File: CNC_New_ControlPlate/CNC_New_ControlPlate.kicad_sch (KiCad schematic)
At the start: 5 parts, among them J1 OTHER

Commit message: [*] Исправлены ошибки с выходами питания. [+] Добавлены обозначения элементов
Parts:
- gave numbers to parts that had none: 4
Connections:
- no-connect marks 0 -> 22

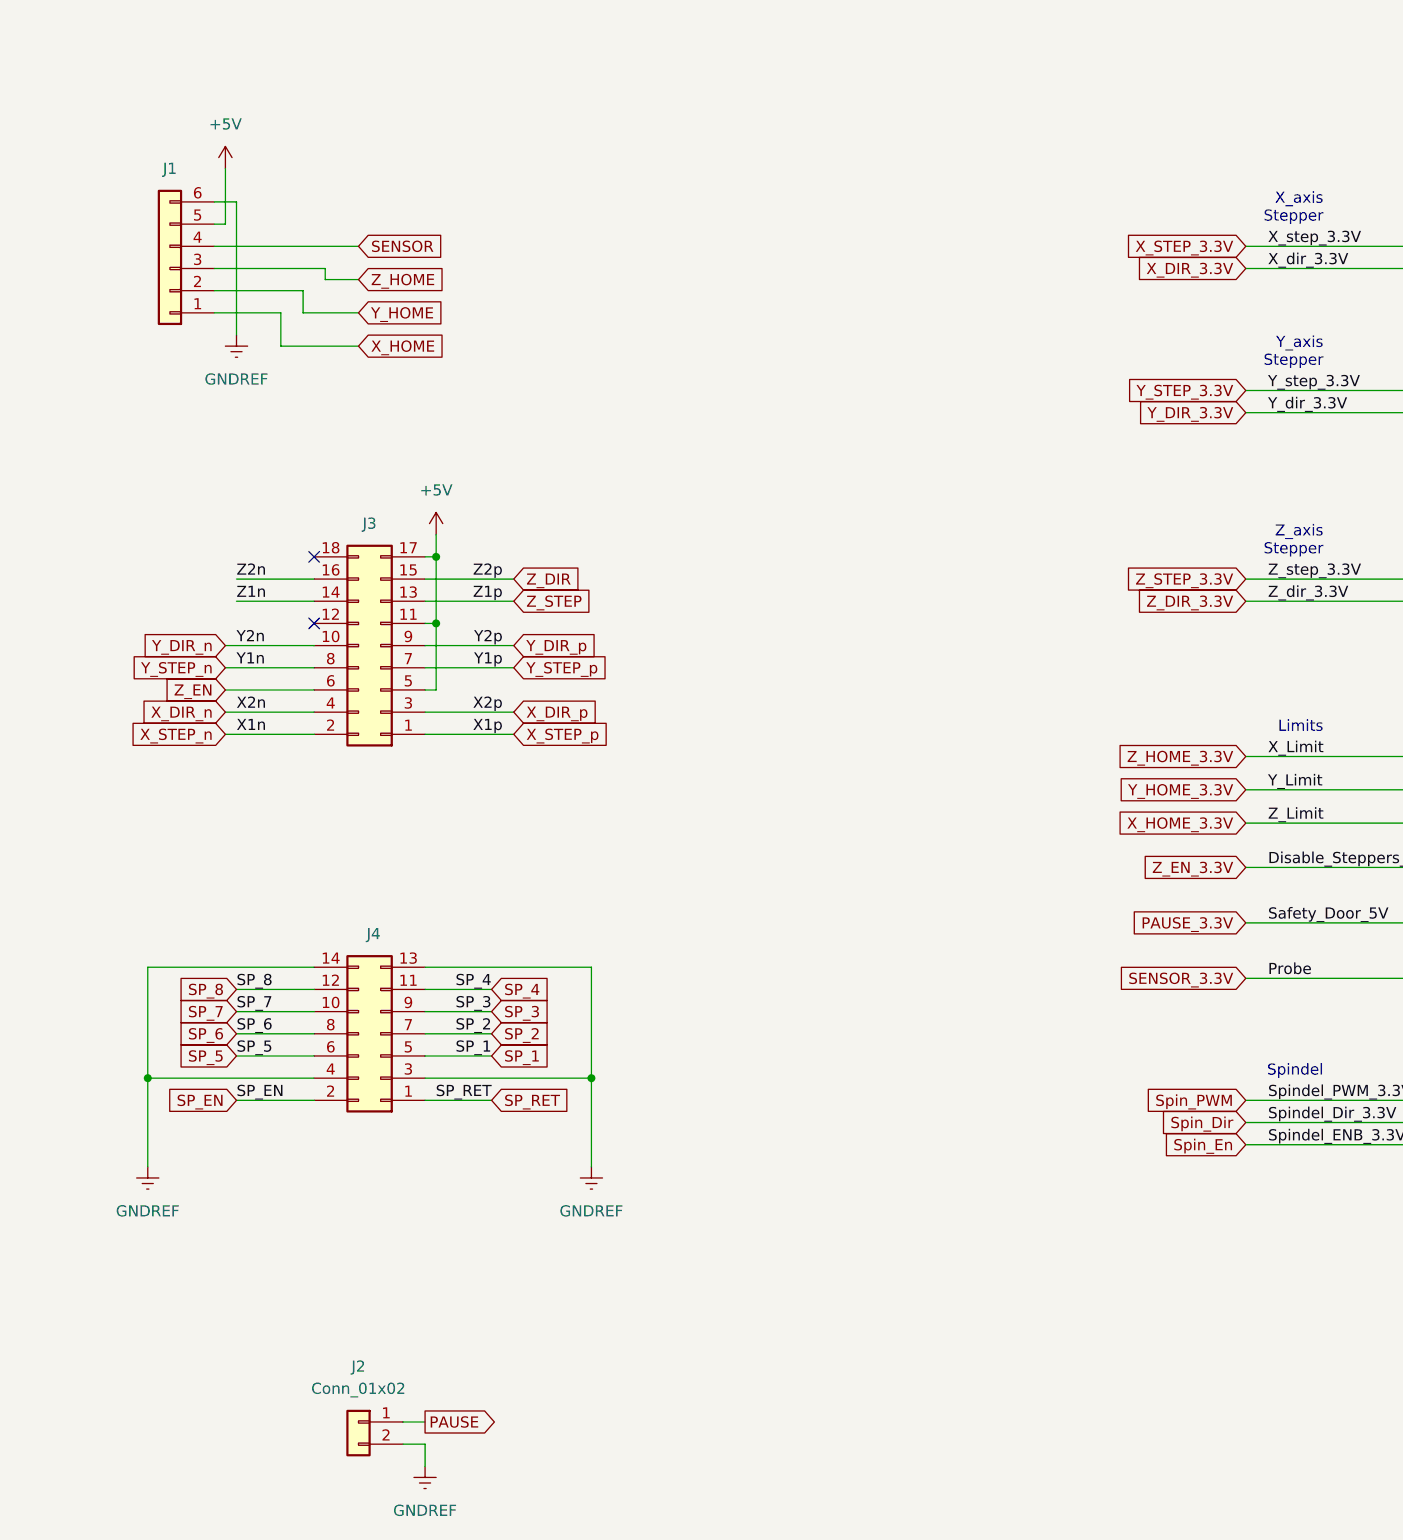
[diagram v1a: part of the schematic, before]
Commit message: [*] Порядок выводов на разъёме Others [*] Порядок выводов на разъёме Pause [*] Порядок подключения каналов на драйвере диф. линий [+] Начата расстановка pcb схемы
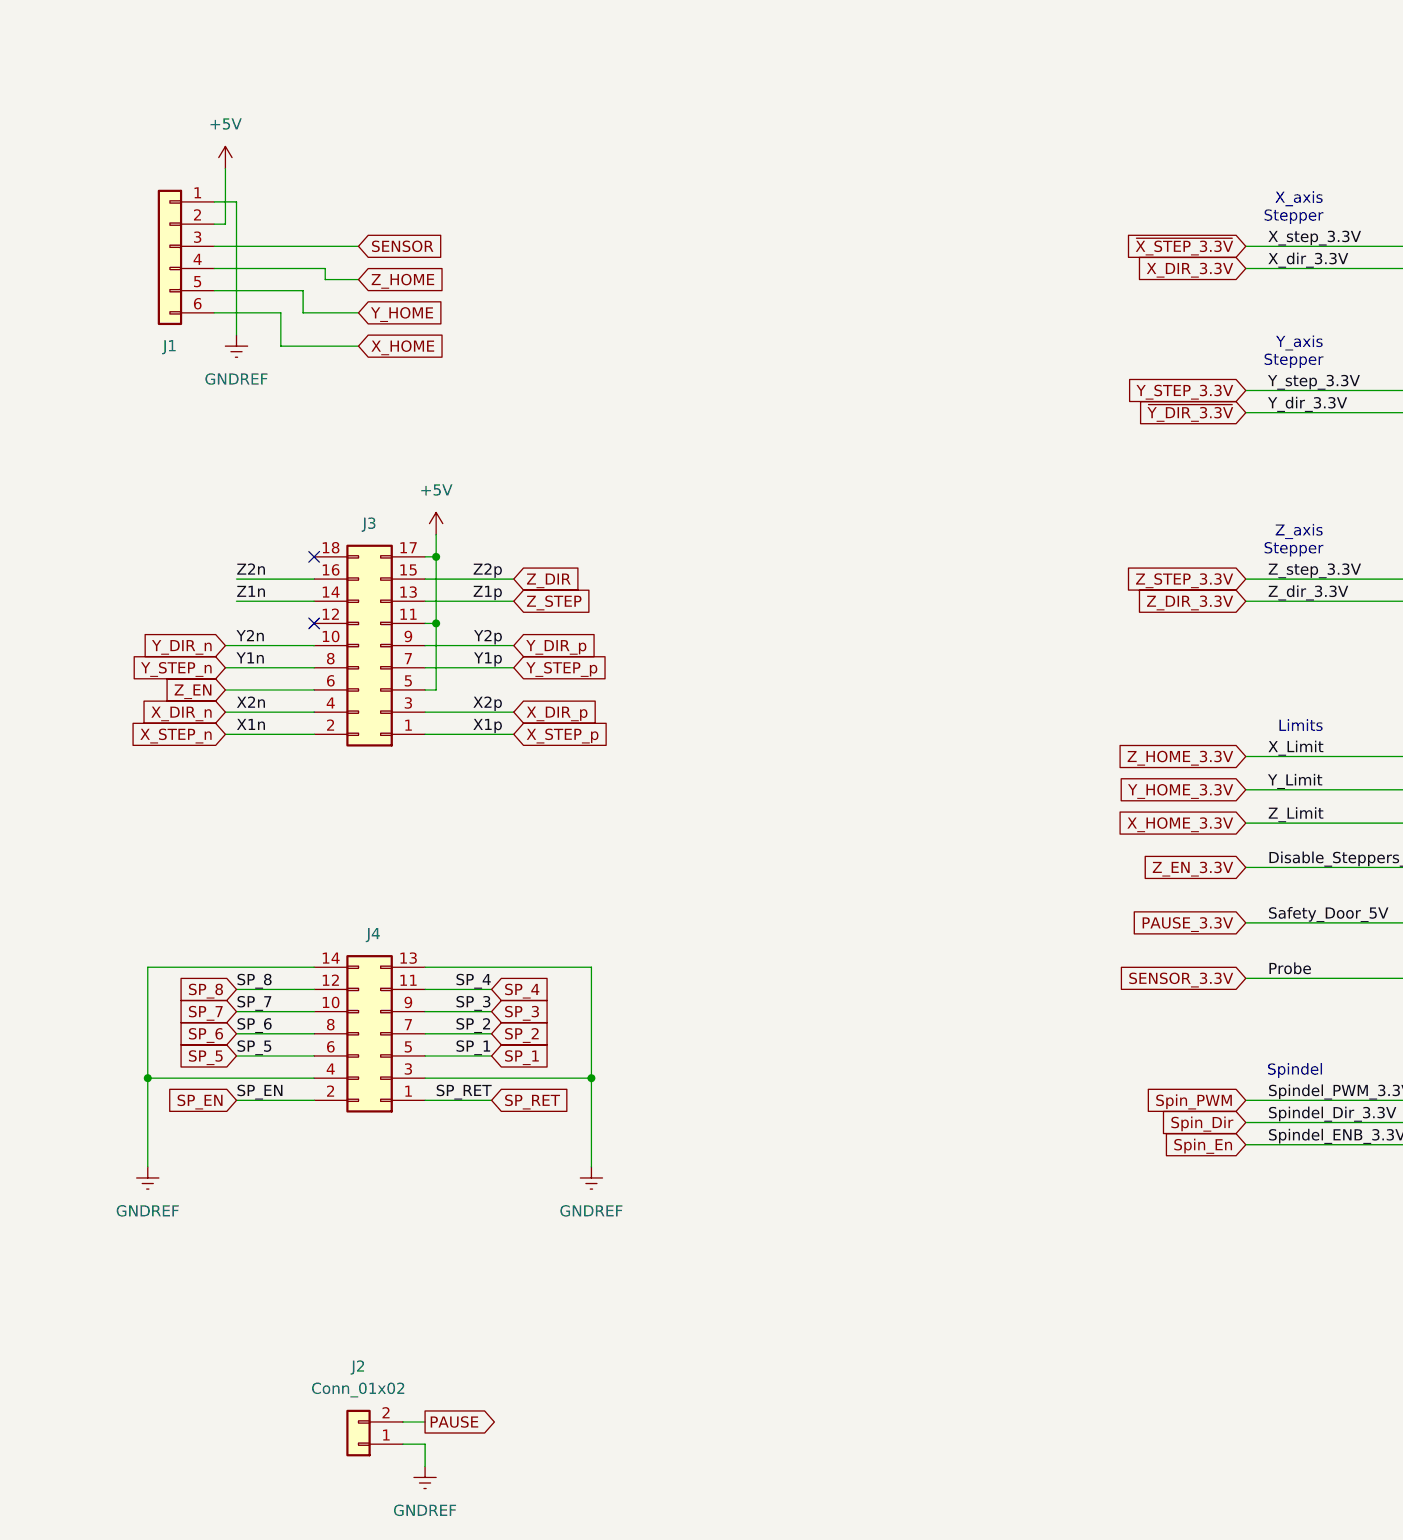
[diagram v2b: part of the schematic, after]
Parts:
- J1: footprint (none) -> Connector_JST:JST_XH_B6B-XH-A_1x06_P2.50mm_Vertical
- J2: footprint (none) -> Connector_JST:JST_XH_B2B-XH-A_1x02_P2.50mm_Vertical
- J3: footprint (none) -> Connector_PinHeader_2.54mm:PinHeader_2x09_P2.54mm_Vertical
- J4: footprint (none) -> Connector_PinHeader_2.54mm:PinHeader_2x07_P2.54mm_Vertical
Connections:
- net +5V: now also J1.2 (Pin_2); no longer J1.5 (Pin_5)
- net GNDREF: now also J1.1 (Pin_1), J2.1 (Pin_1); no longer J1.6 (Pin_6), J2.2 (Pin_2)
- net PAUSE: now also J2.2 (Pin_2); no longer J2.1 (Pin_1)
- net SENSOR: now also J1.3 (Pin_3); no longer J1.4 (Pin_4)
- net X_HOME: now also J1.6 (Pin_6); no longer J1.1 (Pin_1)
- net Y_HOME: now also J1.5 (Pin_5); no longer J1.2 (Pin_2)
- net Z_HOME: now also J1.4 (Pin_4); no longer J1.3 (Pin_3)
- net X_STEP_3.3V renamed ~{X_STEP_3.3V}
- net Y_DIR_3.3V renamed ~{Y_DIR_3.3V}
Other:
- moved on the sheet: J1, J2
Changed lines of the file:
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@@
     )
   )
-  (global_label "Y_DIR_3.3V" (shape input) (at 154.94 50.8 180) (fields_autoplaced)
+  (global_label "~{Y_DIR_3.3V}" (shape input) (at 154.94 50.8 180) (fields_autoplaced)
     (effects (font (size 1.27 1.27)) (justify right))
     (property "Intersheet References" "${INTERSHEET_REFS}" (id 0) (at 142.2459 50.7206 0)
@@
     )
   )
-  (global_label "X_STEP_3.3V" (shape input) (at 154.94 31.75 180) (fields_autoplaced)
+  (global_label "~{X_STEP_3.3V}" (shape input) (at 154.94 31.75 180) (fields_autoplaced)
     (effects (font (size 1.27 1.27)) (justify right))
     (property "Intersheet References" "${INTERSHEET_REFS}" (id 0) (at 140.6736 31.6706 0)
@@
       (effects (font (size 1.27 1.27)) (justify left) hide)
     )
-    (property "Footprint" "" (id 2) (at 55.88 121.92 0)
+    (property "Footprint" "Connector_PinHeader_2.54mm:PinHeader_2x07_P2.54mm_Vertical" (id 2) (at 55.88 121.92 0)
       (effects (font (size 1.27 1.27)) hide)
     )
@@
     (pin "1")
   )
-  (symbol (lib_id "Connector_Generic:Conn_01x02") (at 53.34 166.37 0) (mirror y) (unit 1)
+  (symbol (lib_id "Connector_Generic:Conn_01x02") (at 53.34 168.91 180) (unit 1)
     (in_bom yes) (on_board yes) (fields_autoplaced)
     (property "Reference" "J2" (id 0) (at 53.34 160.02 0))
     (property "Value" "Conn_01x02" (id 1) (at 53.34 162.56 0))
-    (property "Footprint" "" (id 2) (at 53.34 166.37 0)
-      (effects (font (size 1.27 1.27)) hide)
-    )
-    (property "Datasheet" "~" (id 3) (at 53.34 166.37 0)
+    (property "Footprint" "Connector_JST:JST_XH_B2B-XH-A_1x02_P2.50mm_Vertical" (id 2) (at 53.34 168.91 0)
+      (effects (font (size 1.27 1.27)) hide)
+    )
+    (property "Datasheet" "~" (id 3) (at 53.34 168.91 0)
       (effects (font (size 1.27 1.27)) hide)
     )
@@
     (pin "1")
   )
-  (symbol (lib_id "Connector_Generic:Conn_01x06") (at 31.75 34.29 180) (unit 1)
+  (symbol (lib_id "Connector_Generic:Conn_01x06") (at 31.75 31.75 0) (mirror y) (unit 1)
     (in_bom yes) (on_board yes)
-    (property "Reference" "J1" (id 0) (at 31.75 22.86 0))
-    (property "Value" "OTHER" (id 1) (at 31.75 22.86 0)
-      (effects (font (size 1.27 1.27)) hide)
-    )
-    (property "Footprint" "" (id 2) (at 31.75 34.29 0)
-      (effects (font (size 1.27 1.27)) hide)
-    )
-    (property "Datasheet" "~" (id 3) (at 31.75 34.29 0)
+    (property "Reference" "J1" (id 0) (at 31.75 43.18 0))
+    (property "Value" "OTHER" (id 1) (at 31.75 43.18 0)
+      (effects (font (size 1.27 1.27)) hide)
+    )
+    (property "Footprint" "Connector_JST:JST_XH_B6B-XH-A_1x06_P2.50mm_Vertical" (id 2) (at 31.75 31.75 0)
+      (effects (font (size 1.27 1.27)) hide)
+    )
+    (property "Datasheet" "~" (id 3) (at 31.75 31.75 0)
       (effects (font (size 1.27 1.27)) hide)
     )
@@
       (effects (font (size 1.27 1.27)) hide)
     )
-    (property "Footprint" "" (id 2) (at 55.88 77.47 0)
+    (property "Footprint" "Connector_PinHeader_2.54mm:PinHeader_2x09_P2.54mm_Vertical" (id 2) (at 55.88 77.47 0)
       (effects (font (size 1.27 1.27)) hide)
     )
@@
     )
     (path "/bed6146f-bd23-4c63-989f-3dd1365a106a"
-      (reference "J1") (unit 1) (value "OTHER") (footprint "")
+      (reference "J1") (unit 1) (value "OTHER") (footprint "Connector_JST:JST_XH_B6B-XH-A_1x06_P2.50mm_Vertical")
     )
     (path "/533c6d71-5a49-48b1-8a79-9eeec587b167"
-      (reference "J2") (unit 1) (value "Conn_01x02") (footprint "")
+      (reference "J2") (unit 1) (value "Conn_01x02") (footprint "Connector_JST:JST_XH_B2B-XH-A_1x02_P2.50mm_Vertical")
     )
     (path "/dea26430-4380-44d1-9394-b9619f5a7ab8"
-      (reference "J3") (unit 1) (value "STEPPERS") (footprint "")
+      (reference "J3") (unit 1) (value "STEPPERS") (footprint "Connector_PinHeader_2.54mm:PinHeader_2x09_P2.54mm_Vertical")
     )
     (path "/140f3c51-9347-4b10-9448-8e6b70483969"
-      (reference "J4") (unit 1) (value "SPINDEL") (footprint "")
+      (reference "J4") (unit 1) (value "SPINDEL") (footprint "Connector_PinHeader_2.54mm:PinHeader_2x07_P2.54mm_Vertical")
     )
     (path "/07e4ffe7-a231-410f-8aa1-cd8347b537a5/8c9aa3a4-c2cf-4c05-9701-54980603a114"
@@
     )
     (path "/f81b86d1-c1b9-4e8d-8ec5-902244442743/824fe6e1-ae2e-42d4-9518-ebc7c8181ef9"
-      (reference "R11") (unit 1) (value "10k") (footprint "")
+      (reference "R11") (unit 1) (value "10k") (footprint "Resistor_SMD:R_0603_1608Metric")
     )
     (path "/07e4ffe7-a231-410f-8aa1-cd8347b537a5/8249b123-3867-4005-86be-14bfa774027c"
@@
     )
     (path "/cddb5583-7ddf-474c-aeca-fbc0e04243fc/5073a31c-56c7-4a11-a025-f6ad24fd7dbb"
-      (reference "U3") (unit 1) (value "7406") (footprint "")
+      (reference "U3") (unit 1) (value "7406") (footprint "Package_DIP:DIP-14_W7.62mm_Socket")
     )
     (path "/cddb5583-7ddf-474c-aeca-fbc0e04243fc/3d75ff4a-fbad-4181-b5f4-65bd16a4fd34"
-      (reference "U3") (unit 2) (value "7406") (footprint "")
+      (reference "U3") (unit 2) (value "7406") (footprint "Package_DIP:DIP-14_W7.62mm_Socket")
     )
     (path "/cddb5583-7ddf-474c-aeca-fbc0e04243fc/fab1d4b5-7f40-4e7c-a269-5493418d8603"
-      (reference "U3") (unit 3) (value "7406") (footprint "")
+      (reference "U3") (unit 3) (value "7406") (footprint "Package_DIP:DIP-14_W7.62mm_Socket")
     )
     (path "/f81b86d1-c1b9-4e8d-8ec5-902244442743/3f9cb9c7-b074-445a-bba0-4cc017ec9b22"
-      (reference "U3") (unit 4) (value "7406") (footprint "")
+      (reference "U3") (unit 4) (value "7406") (footprint "Package_DIP:DIP-14_W7.62mm_Socket")
     )
     (path "/f81b86d1-c1b9-4e8d-8ec5-902244442743/eb052de6-58fb-4391-b769-3bb4c691f811"
-      (reference "U3") (unit 5) (value "7406") (footprint "")
+      (reference "U3") (unit 5) (value "7406") (footprint "Package_DIP:DIP-14_W7.62mm_Socket")
     )
     (path "/f81b86d1-c1b9-4e8d-8ec5-902244442743/32852d4f-6ab0-4f52-8f49-8b7e66e79f8d"
-      (reference "U3") (unit 6) (value "7406") (footprint "")
+      (reference "U3") (unit 6) (value "7406") (footprint "Package_DIP:DIP-14_W7.62mm_Socket")
     )
     (path "/f81b86d1-c1b9-4e8d-8ec5-902244442743/9f735f94-c12e-4d19-924f-16af0f881e41"
@@
     )
     (path "/f81b86d1-c1b9-4e8d-8ec5-902244442743/a95f66a3-1299-49c3-9845-b9159b1bfeaa"
-      (reference "Y1") (unit 1) (value "4MHz") (footprint "")
-    )
-  )
+      (reference "Y1") (unit 1) (value "4MHz") (footprint "Crystal:Crystal_HC49-4H_Vertical")
+    )
+  )
